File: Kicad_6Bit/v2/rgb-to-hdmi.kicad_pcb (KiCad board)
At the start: 2 copper layers, 65 x 30 mm, 31 parts, among them J1 Conn_01x03, P1 CONN_02X20, P2 Conn_02x05_Odd_Even, P3 Conn_01x06, P4 CONN_01X02, SW1 SW_PUSH, SW2 SW_PUSH, SW3 SW_PUSH, SW4 SW_PUSH, U1 XC9572XL-VQFP44

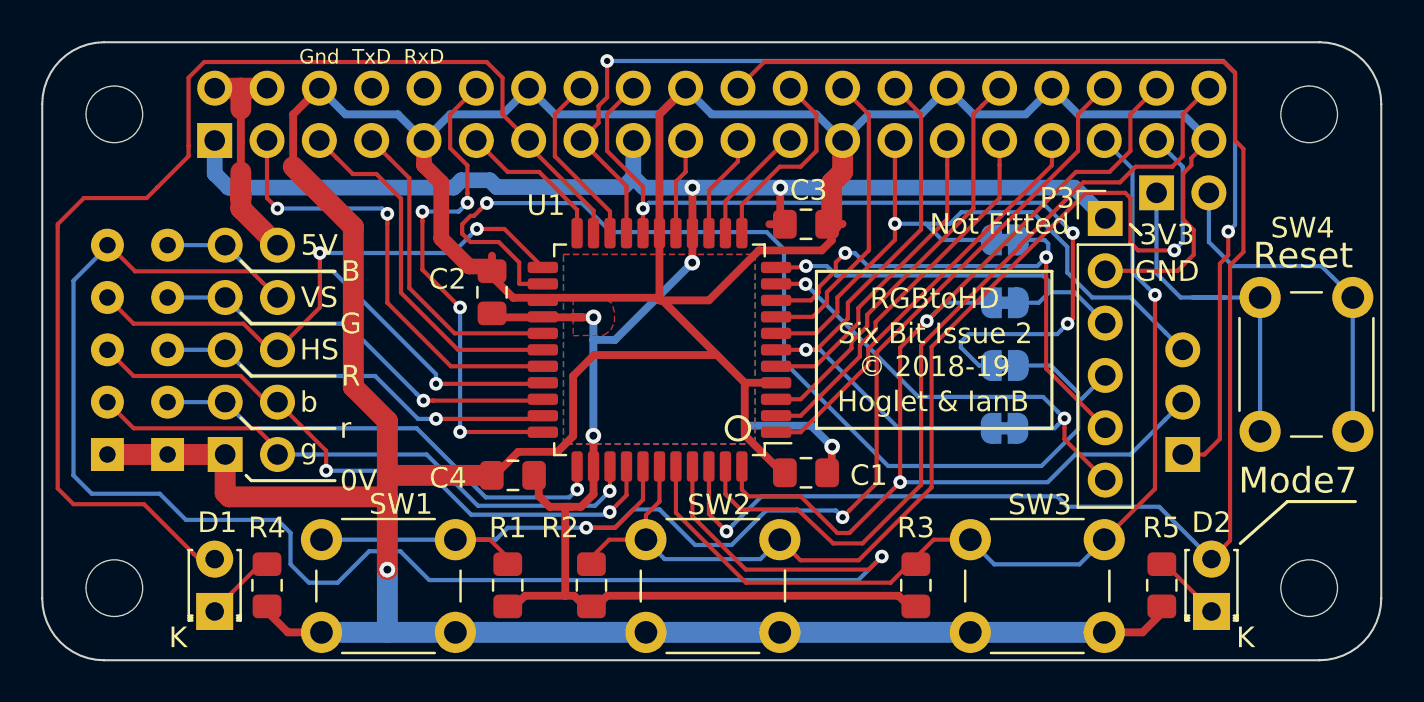
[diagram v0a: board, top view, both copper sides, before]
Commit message: Move 3 pin data header
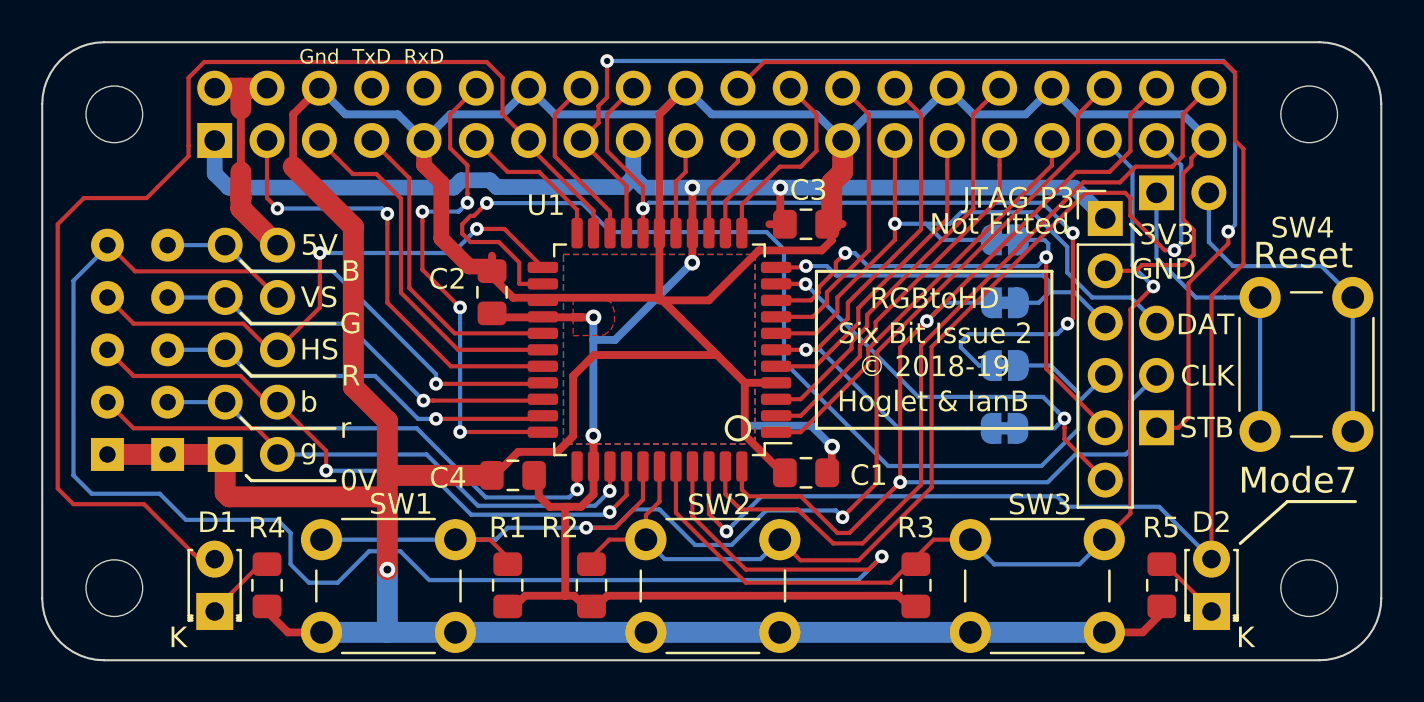
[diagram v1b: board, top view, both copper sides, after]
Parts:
- moved J1 1.81 mm to (66.6, 43.2)
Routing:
- net Net-(P4-Pad1): track 17.9 -> 15.9 mm
- net /GPIO0: track 34.1 -> 32.3 mm
- net /GPIO26: track 53.5 -> 52.7 mm
- net /GPIO22: track 61.0 -> 60.3 mm
- net /GPIO20: track 54.3 -> 54.9 mm
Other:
- board text added: "CLK"
- board text added: "DAT"
- board text added: "JTAG"
- board text added: "STB"

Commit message: Add P19 pin
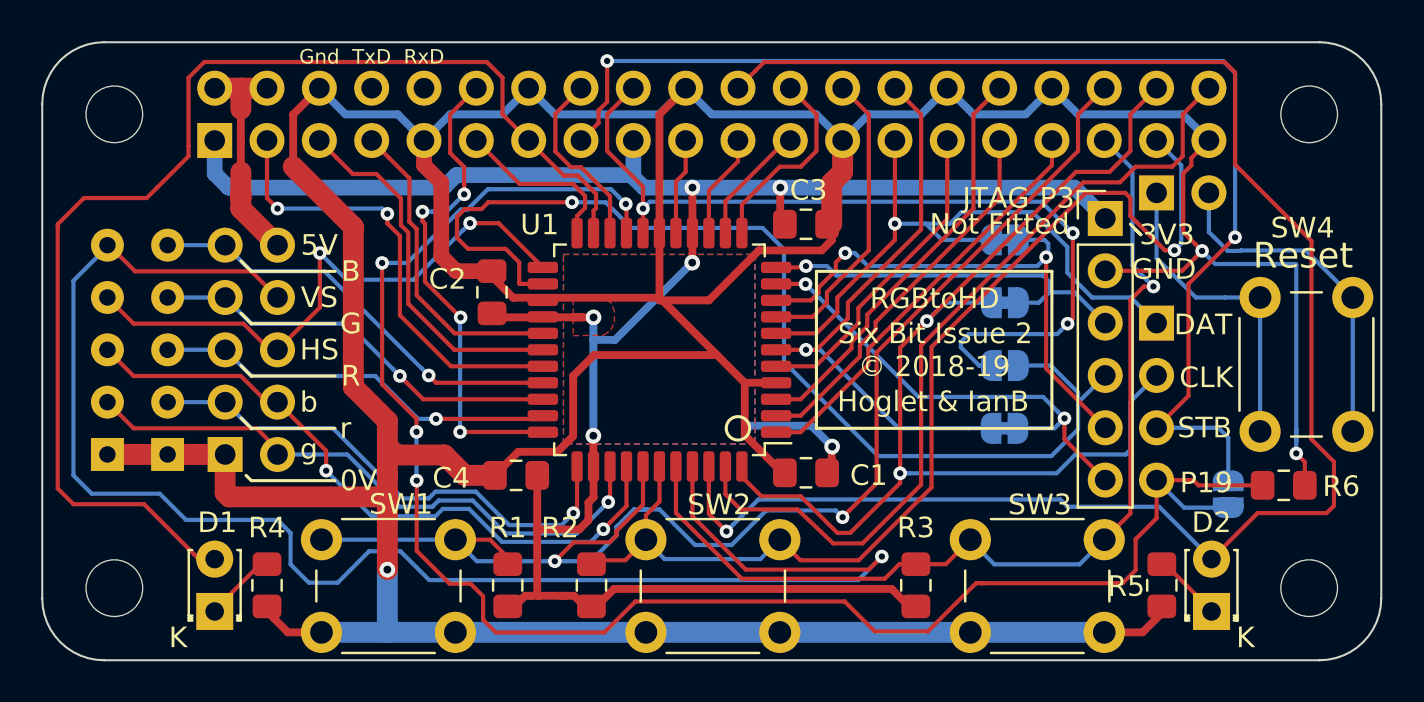
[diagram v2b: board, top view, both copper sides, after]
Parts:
- removed J1: Conn_01x03, Connector_PinSocket_2.54mm:PinSocket_1x03_P2.54mm_Vertical
- added JP5: SolderJumper_2_Open, Jumper:SolderJumper-2_P1.3mm_Open_RoundedPad1.0x1.5mm, B.Cu at (70.1, 46.4)
- added P5: Conn_01x04, Connector_PinSocket_2.54mm:PinSocket_1x04_P2.54mm_Vertical, B.Cu at (66.6, 38.1)
- added R6: 2K2, Resistor_SMD:R_0805_2012Metric_Pad1.15x1.40mm_HandSolder, F.Cu at (72.8, 46.0)
- R1, R2, R3: value 4K7 -> 1K
- RN1, RN2: value 4.7K -> 2K2
- moved C4 0.15 mm to (35.5, 45.5)
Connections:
- U1 pad 19: /GPIO22 -> /SPARE
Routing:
- net /SPARE: track 0.00 -> 83.9 mm, vias 0 -> 4
- net /GND: track 227.1 -> 244.6 mm, vias 1 -> 3
- net /GPIO25: track 78.1 -> 83.6 mm
- net /GPIO16: track 62.0 -> 65.8 mm
- net /BRED: track 23.1 -> 25.0 mm
- net /BGREEN: track 27.9 -> 29.8 mm
- net /BBLUE: track 30.1 -> 32.0 mm
- net /SYNC: track 27.0 -> 28.3 mm
- net /GPIO17: track 7.23 -> 8.36 mm
- net /GPIO27: track 58.4 -> 59.1 mm
- net /GPIO20: track 54.9 -> 54.4 mm
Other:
- board text added: "P19"
- board text removed: "Mode7"

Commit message: Change CLK to CLKEN
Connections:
- P5 pad 2: /GPIO20 -> /GPIO1
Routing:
- net /GPIO20: track 54.4 -> 38.6 mm, vias 2 -> 1
- net /GPIO1: track 27.7 -> 42.7 mm, vias 1 -> 3

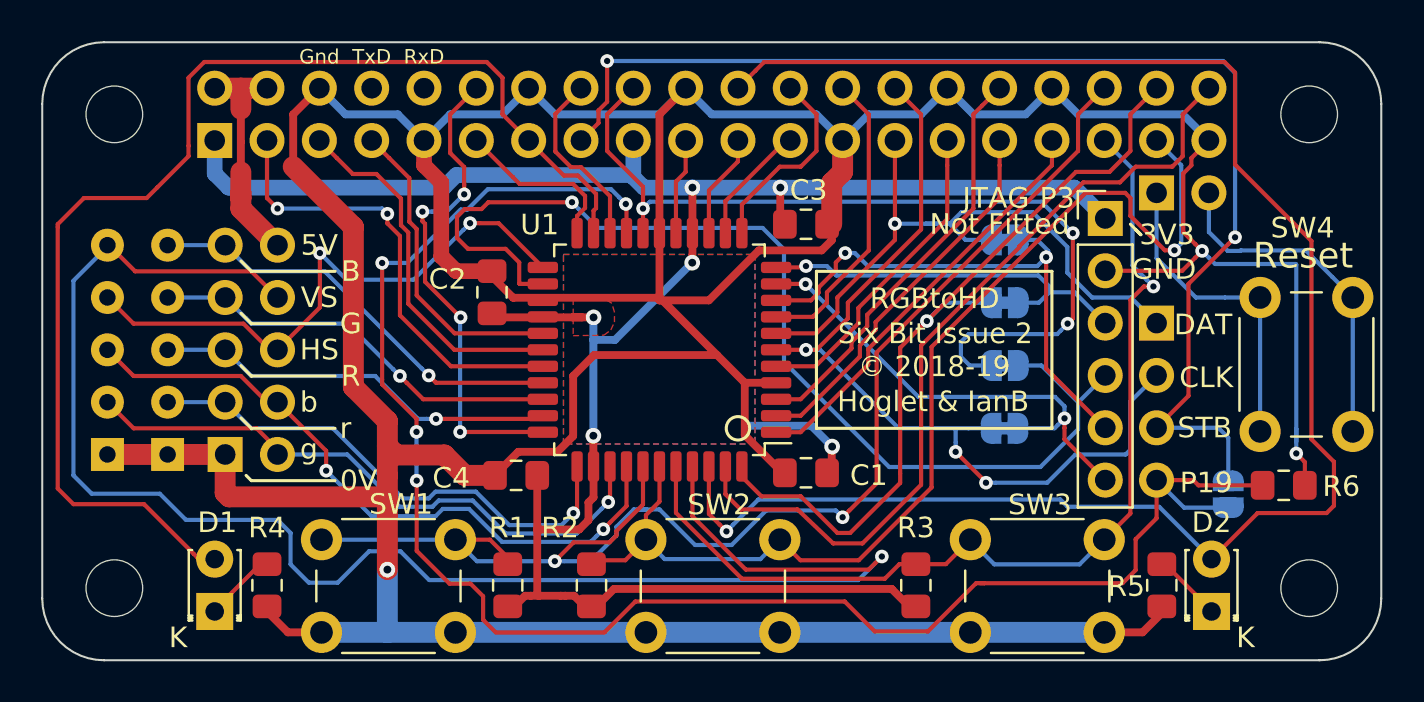
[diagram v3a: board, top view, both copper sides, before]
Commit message: Move RGB connector
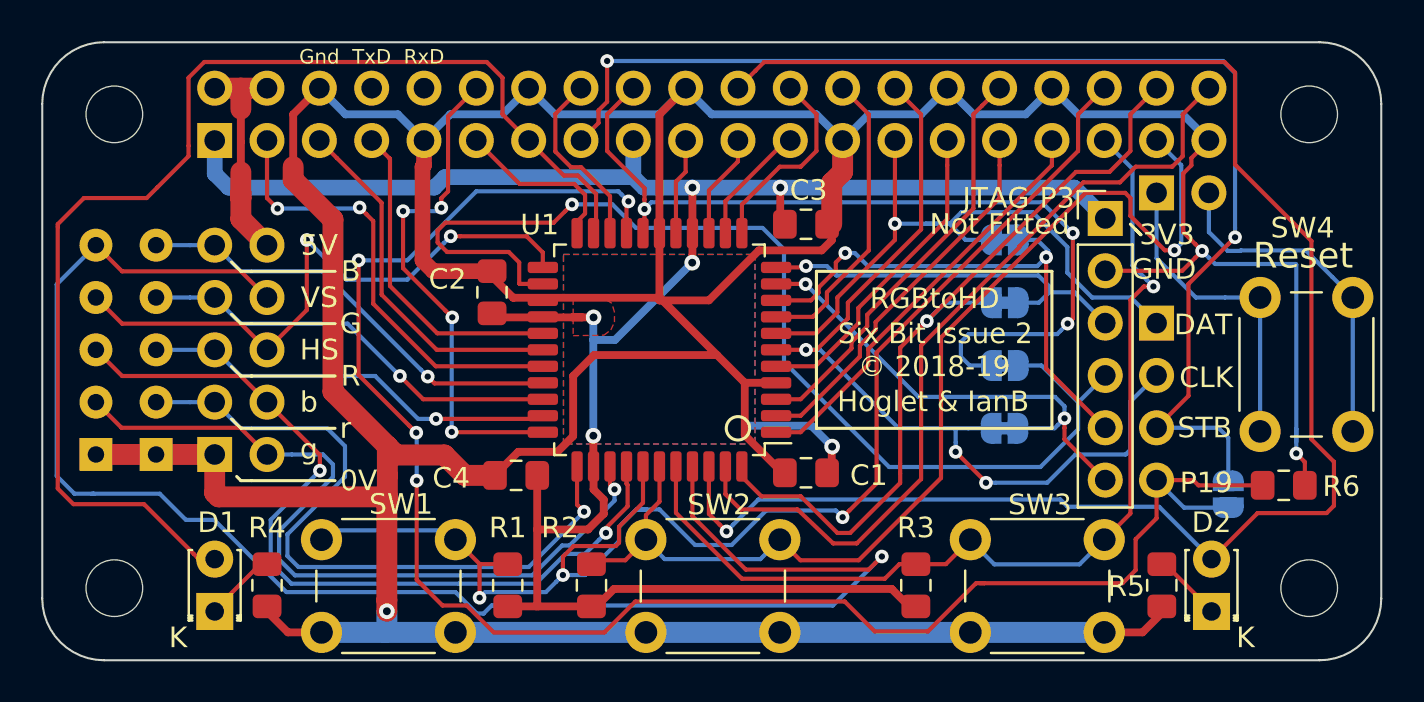
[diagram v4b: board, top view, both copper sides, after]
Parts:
- moved RN2 0.56 mm to (15.1, 44.5)
- moved RN1 0.56 mm to (18.0, 44.5)
- moved P2 0.51 mm to (20.9, 44.5)
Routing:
- net /BRED: track 25.0 -> 34.6 mm
- net /BGREEN: track 29.8 -> 38.7 mm
- net /BBLUE: track 32.0 -> 40.7 mm
- net /SYNC: track 28.3 -> 30.3 mm
- net /SPARE: track 83.9 -> 85.9 mm
- net /GND: track 244.6 -> 246.4 mm
- net /GPIO16: track 65.8 -> 67.5 mm, vias 2 -> 3
- net /TDO: track 53.1 -> 54.7 mm
- net /GPIO18: track 23.8 -> 24.6 mm
- net /BLUE: track 20.8 -> 21.4 mm
- net /GREEN: track 20.3 -> 20.8 mm
- net /RED: track 19.5 -> 20.0 mm

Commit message: Change value of R5 from 2K2 to 10K
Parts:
- R6: value 2K2 -> 10K
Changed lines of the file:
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@@
       (effects (font (size 1 1) (thickness 0.15)))
     )
-    (fp_text value 2K2 (at 0 1.65) (layer F.Fab)
+    (fp_text value 10K (at 0 1.65) (layer F.Fab)
       (effects (font (size 1 1) (thickness 0.15)))
     )

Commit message: Change RN1&2 to 4K7
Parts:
- RN1, RN2: value 2K2 -> 4K7
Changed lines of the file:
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@@
       (effects (font (size 1 1) (thickness 0.15)) (justify mirror))
     )
-    (fp_text value 2K2 (at 6.35 -2.4 90) (layer B.Fab)
+    (fp_text value 4K7 (at 6.35 -2.4 90) (layer B.Fab)
       (effects (font (size 1 1) (thickness 0.15)) (justify mirror))
     )
@@
       (effects (font (size 1 1) (thickness 0.15)) (justify mirror))
     )
-    (fp_text value 2K2 (at 6.35 -2.4 90) (layer B.Fab)
-      (effects (font (size 1 1) (thickness 0.15)) (justify mirror))
-    )
+    (fp_text value 4K7 (at 6.35 -2.4 90) (layer B.Fab)
+      (effects (font (size 1 1) (thickness 0.15)) (justify mirror))
+    )
